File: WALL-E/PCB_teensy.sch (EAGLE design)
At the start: 50 parts

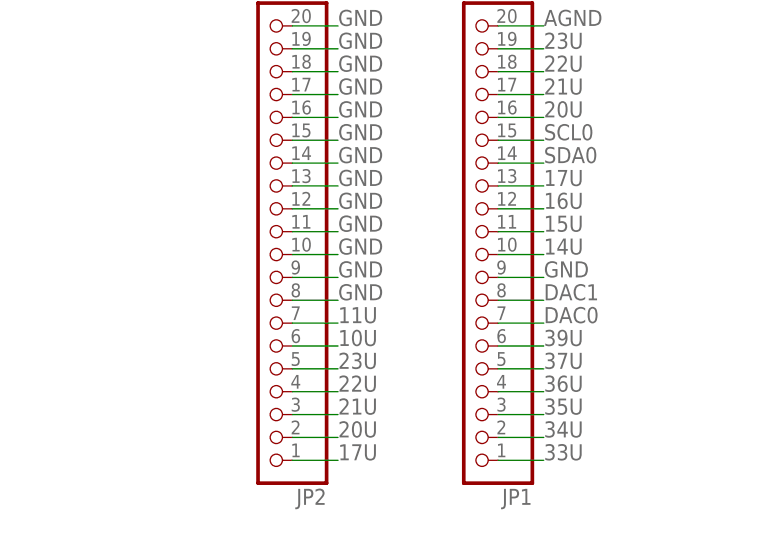
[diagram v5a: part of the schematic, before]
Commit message: Rewired the pins for JP2 to make the pins be physically closer to the teensy.
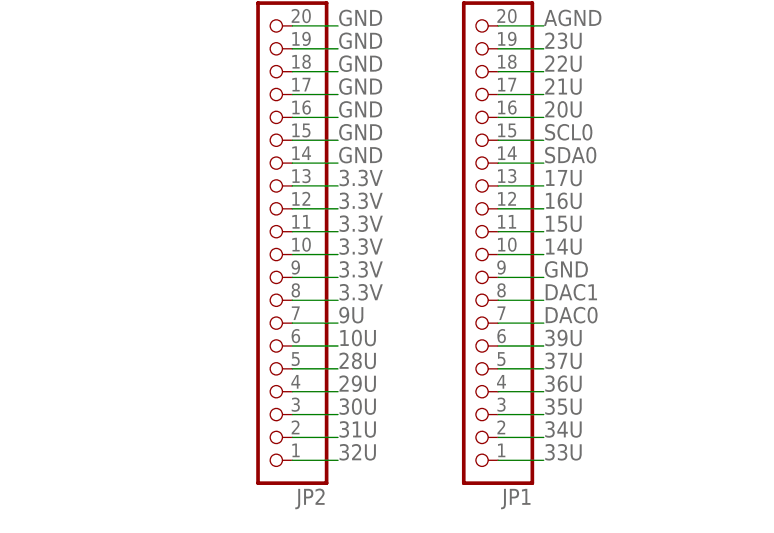
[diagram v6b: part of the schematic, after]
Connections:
- net 11U: no longer JP2.7
- net 17U: no longer JP2.1
- net 20U: no longer JP2.2
- net 21U: no longer JP2.3
- net 22U: no longer JP2.4
- net 23U: no longer JP2.5
- net 28U: now also JP2.5
- net 29U: now also JP2.4
- net 3.3V: now also JP2.10, JP2.11, JP2.12, JP2.13, JP2.8, JP2.9
- net 30U: now also JP2.3
- net 31U: now also JP2.2
- net 32U: now also JP2.1
- net 9U: now also JP2.7
- net GND: no longer JP2.10, JP2.11, JP2.12, JP2.13, JP2.8, JP2.9
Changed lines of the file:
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@@
-</segment>
-<segment>
-<pinref part="JP2" gate="A" pin="8"/>
-<wire x1="-96.52" y1="-35.56" x2="-91.44" y2="-35.56" width="0.1524" layer="91"/>
-<label x="-91.44" y="-35.56" size="1.778" layer="95"/>
-</segment>
-<segment>
-<wire x1="-96.52" y1="-33.02" x2="-91.44" y2="-33.02" width="0.1524" layer="91"/>
-<label x="-91.44" y="-33.02" size="1.778" layer="95"/>
-<pinref part="JP2" gate="A" pin="9"/>
-</segment>
-<segment>
-<wire x1="-96.52" y1="-30.48" x2="-91.44" y2="-30.48" width="0.1524" layer="91"/>
-<label x="-91.44" y="-30.48" size="1.778" layer="95"/>
-<pinref part="JP2" gate="A" pin="10"/>
-</segment>
-<segment>
-<wire x1="-96.52" y1="-27.94" x2="-91.44" y2="-27.94" width="0.1524" layer="91"/>
-<label x="-91.44" y="-27.94" size="1.778" layer="95"/>
-<pinref part="JP2" gate="A" pin="11"/>
-</segment>
-<segment>
-<wire x1="-96.52" y1="-25.4" x2="-91.44" y2="-25.4" width="0.1524" layer="91"/>
-<label x="-91.44" y="-25.4" size="1.778" layer="95"/>
-<pinref part="JP2" gate="A" pin="12"/>
-</segment>
-<segment>
-<wire x1="-96.52" y1="-22.86" x2="-91.44" y2="-22.86" width="0.1524" layer="91"/>
-<label x="-91.44" y="-22.86" size="1.778" layer="95"/>
-<pinref part="JP2" gate="A" pin="13"/>
 </segment>
 <segment>
@@
 <label x="78.74" y="60.96" size="1.778" layer="95"/>
 </segment>
+<segment>
+<pinref part="JP2" gate="A" pin="8"/>
+<wire x1="-96.52" y1="-35.56" x2="-91.44" y2="-35.56" width="0.1524" layer="91"/>
+<label x="-91.44" y="-35.56" size="1.778" layer="95"/>
+</segment>
+<segment>
+<wire x1="-96.52" y1="-33.02" x2="-91.44" y2="-33.02" width="0.1524" layer="91"/>
+<label x="-91.44" y="-33.02" size="1.778" layer="95"/>
+<pinref part="JP2" gate="A" pin="9"/>
+</segment>
+<segment>
+<wire x1="-96.52" y1="-30.48" x2="-91.44" y2="-30.48" width="0.1524" layer="91"/>
+<label x="-91.44" y="-30.48" size="1.778" layer="95"/>
+<pinref part="JP2" gate="A" pin="10"/>
+</segment>
+<segment>
+<wire x1="-96.52" y1="-27.94" x2="-91.44" y2="-27.94" width="0.1524" layer="91"/>
+<label x="-91.44" y="-27.94" size="1.778" layer="95"/>
+<pinref part="JP2" gate="A" pin="11"/>
+</segment>
+<segment>
+<wire x1="-96.52" y1="-25.4" x2="-91.44" y2="-25.4" width="0.1524" layer="91"/>
+<label x="-91.44" y="-25.4" size="1.778" layer="95"/>
+<pinref part="JP2" gate="A" pin="12"/>
+</segment>
+<segment>
+<wire x1="-96.52" y1="-22.86" x2="-91.44" y2="-22.86" width="0.1524" layer="91"/>
+<label x="-91.44" y="-22.86" size="1.778" layer="95"/>
+<pinref part="JP2" gate="A" pin="13"/>
+</segment>
 </net>
 <net name="N$8" class="0">
@@
 <label x="-35.56" y="15.24" size="1.778" layer="95"/>
 </segment>
+<segment>
+<pinref part="JP2" gate="A" pin="5"/>
+<wire x1="-96.52" y1="-43.18" x2="-91.44" y2="-43.18" width="0.1524" layer="91"/>
+<label x="-91.44" y="-43.18" size="1.778" layer="95"/>
+</segment>
 </net>
 <net name="29U" class="0">
@@
 <label x="-35.56" y="12.7" size="1.778" layer="95"/>
 </segment>
+<segment>
+<pinref part="JP2" gate="A" pin="4"/>
+<wire x1="-96.52" y1="-45.72" x2="-91.44" y2="-45.72" width="0.1524" layer="91"/>
+<label x="-91.44" y="-45.72" size="1.778" layer="95"/>
+</segment>
 </net>
 <net name="30U" class="0">
@@
 <label x="-35.56" y="10.16" size="1.778" layer="95"/>
 </segment>
+<segment>
+<pinref part="JP2" gate="A" pin="3"/>
+<wire x1="-96.52" y1="-48.26" x2="-91.44" y2="-48.26" width="0.1524" layer="91"/>
+<label x="-91.44" y="-48.26" size="1.778" layer="95"/>
+</segment>
 </net>
 <net name="31U" class="0">
@@
 <label x="-35.56" y="7.62" size="1.778" layer="95"/>
 </segment>
+<segment>
+<pinref part="JP2" gate="A" pin="2"/>
+<wire x1="-96.52" y1="-50.8" x2="-91.44" y2="-50.8" width="0.1524" layer="91"/>
+<label x="-91.44" y="-50.8" size="1.778" layer="95"/>
+</segment>
 </net>
 <net name="32U" class="0">
@@
 <label x="-35.56" y="5.08" size="1.778" layer="95"/>
 </segment>
+<segment>
+<pinref part="JP2" gate="A" pin="1"/>
+<wire x1="-96.52" y1="-53.34" x2="-91.44" y2="-53.34" width="0.1524" layer="91"/>
+<label x="-91.44" y="-53.34" size="1.778" layer="95"/>
+</segment>
 </net>
 <net name="33U" class="0">
@@
 </segment>
 <segment>
-<pinref part="JP2" gate="A" pin="1"/>
-<wire x1="-96.52" y1="-53.34" x2="-91.44" y2="-53.34" width="0.1524" layer="91"/>
-<label x="-91.44" y="-53.34" size="1.778" layer="95"/>
-</segment>
-<segment>
 <pinref part="JP1" gate="A" pin="13"/>
 <wire x1="-73.66" y1="-22.86" x2="-68.58" y2="-22.86" width="0.1524" layer="91"/>
@@
 </segment>
 <segment>
-<pinref part="JP2" gate="A" pin="2"/>
-<wire x1="-96.52" y1="-50.8" x2="-91.44" y2="-50.8" width="0.1524" layer="91"/>
-<label x="-91.44" y="-50.8" size="1.778" layer="95"/>
-</segment>
-<segment>
 <pinref part="JP1" gate="A" pin="16"/>
 <wire x1="-73.66" y1="-15.24" x2="-68.58" y2="-15.24" width="0.1524" layer="91"/>
@@
 </segment>
 <segment>
-<pinref part="JP2" gate="A" pin="3"/>
-<wire x1="-96.52" y1="-48.26" x2="-91.44" y2="-48.26" width="0.1524" layer="91"/>
-<label x="-91.44" y="-48.26" size="1.778" layer="95"/>
-</segment>
-<segment>
 <pinref part="JP1" gate="A" pin="17"/>
 <wire x1="-73.66" y1="-12.7" x2="-68.58" y2="-12.7" width="0.1524" layer="91"/>
@@
 </segment>
 <segment>
-<pinref part="JP2" gate="A" pin="4"/>
-<wire x1="-96.52" y1="-45.72" x2="-91.44" y2="-45.72" width="0.1524" layer="91"/>
-<label x="-91.44" y="-45.72" size="1.778" layer="95"/>
-</segment>
-<segment>
 <pinref part="JP1" gate="A" pin="18"/>
 <wire x1="-73.66" y1="-10.16" x2="-68.58" y2="-10.16" width="0.1524" layer="91"/>
@@
 </segment>
 <segment>
-<pinref part="JP2" gate="A" pin="5"/>
-<wire x1="-96.52" y1="-43.18" x2="-91.44" y2="-43.18" width="0.1524" layer="91"/>
-<label x="-91.44" y="-43.18" size="1.778" layer="95"/>
-</segment>
-<segment>
 <pinref part="JP1" gate="A" pin="19"/>
 <wire x1="-73.66" y1="-7.62" x2="-68.58" y2="-7.62" width="0.1524" layer="91"/>
@@
 <label x="-35.56" y="38.1" size="1.778" layer="95"/>
 </segment>
+<segment>
+<pinref part="JP2" gate="A" pin="7"/>
+<wire x1="-96.52" y1="-38.1" x2="-91.44" y2="-38.1" width="0.1524" layer="91"/>
+<label x="-91.44" y="-38.1" size="1.778" layer="95"/>
+</segment>
 </net>
 <net name="10U" class="0">
@@
 <label x="-7.62" y="83.82" size="1.778" layer="95"/>
 </segment>
-<segment>
-<pinref part="JP2" gate="A" pin="7"/>
-<wire x1="-96.52" y1="-38.1" x2="-91.44" y2="-38.1" width="0.1524" layer="91"/>
-<label x="-91.44" y="-38.1" size="1.778" layer="95"/>
-</segment>
-</net>
+</net>

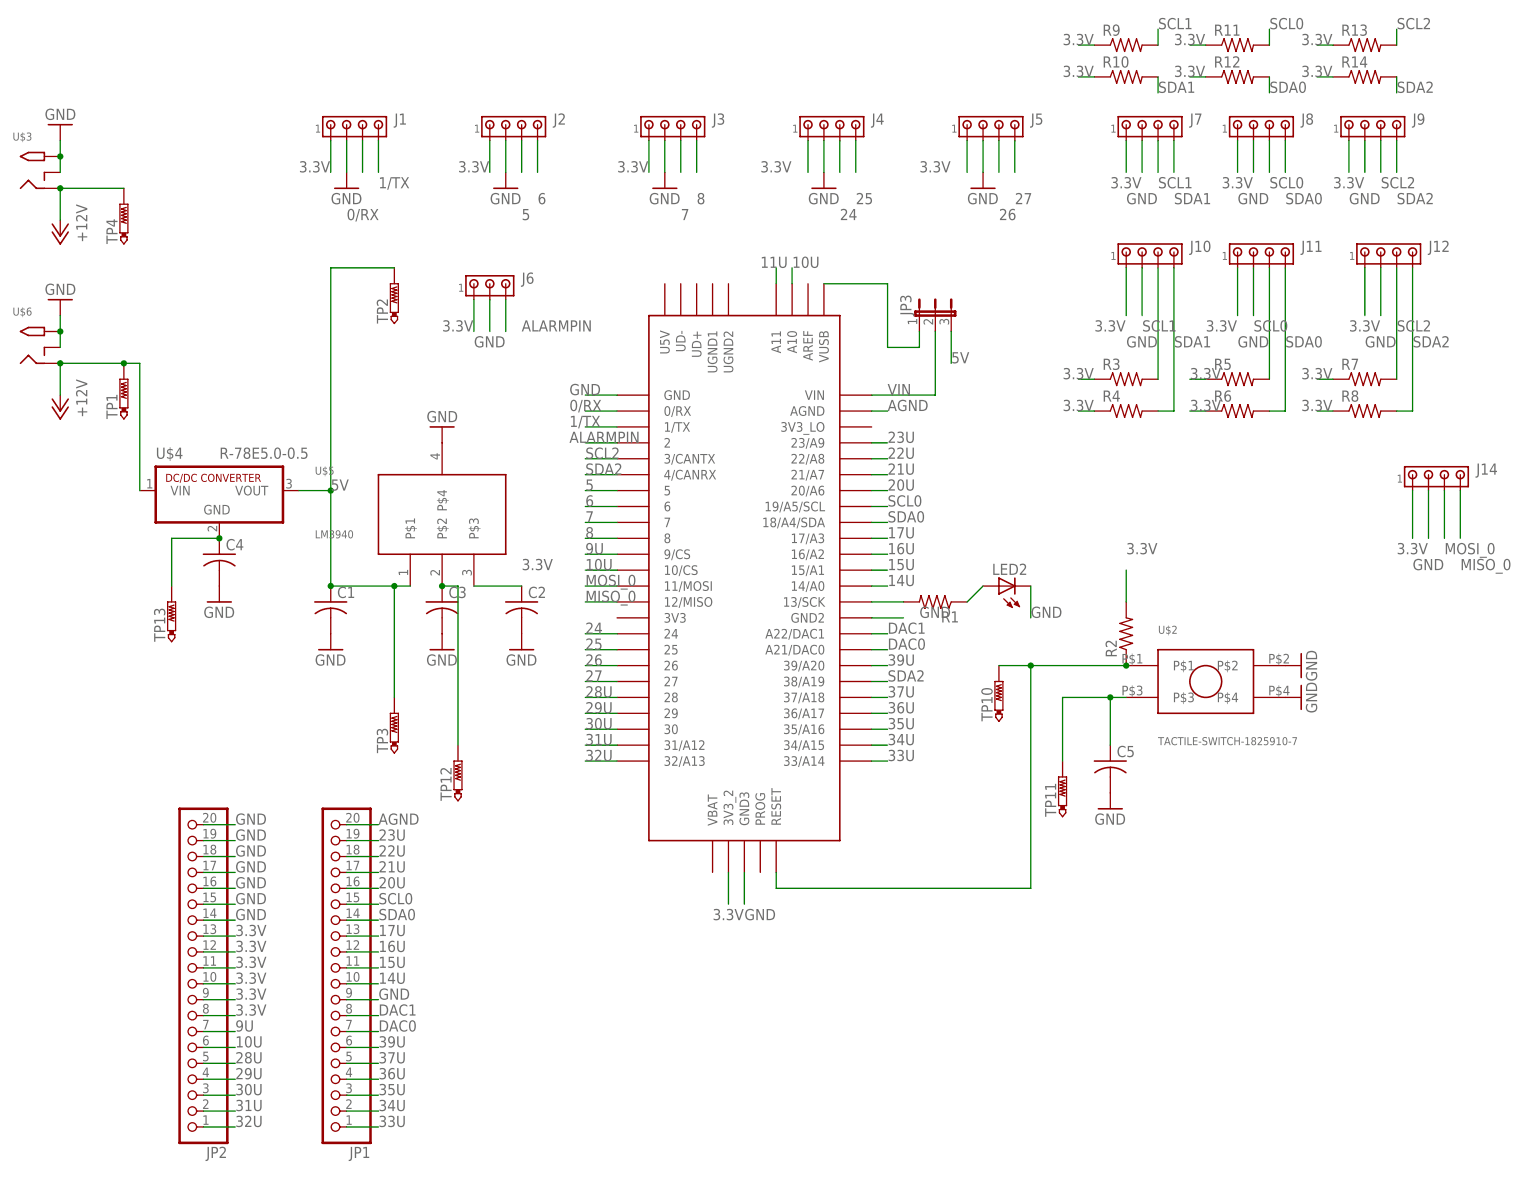
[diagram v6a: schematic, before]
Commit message: Routed all the header pins closest to Teensy and resistors.
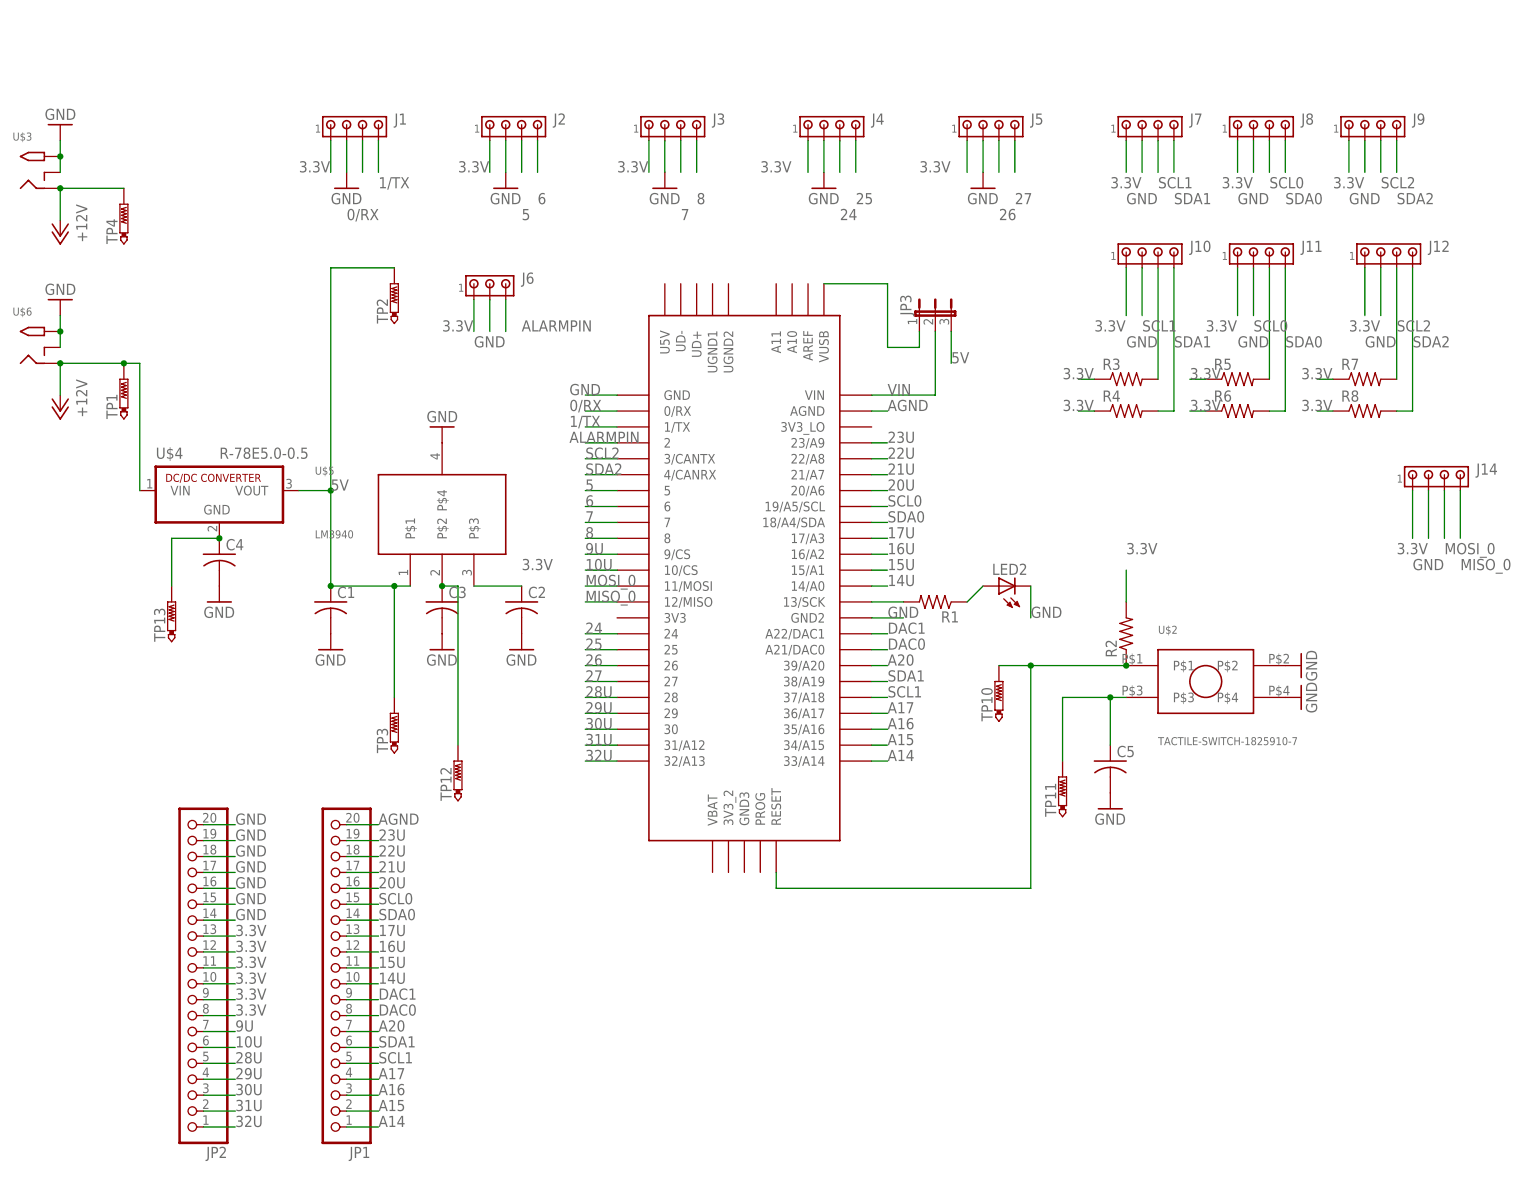
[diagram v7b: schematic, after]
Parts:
- removed R10, R11, R12, R13, R14, R9: (no value), adafruit:R-US_R0805
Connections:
- net 33U renamed A14
- net 34U renamed A15
- net 35U renamed A16
- net 36U renamed A17
- removed net 11U: U$1.A11
- removed net 37U: JP1.5, U$1.37/A18
- removed net 39U: JP1.6, U$1.39/A20
- new net A20: JP1.7, U$1.39/A20
- net 10U: no longer U$1.A10
- net 3.3V: no longer R10.1, R11.1, R12.1, R13.1, R14.1, R9.1, U$1.3V3_2
- net DAC0: now also JP1.8; no longer JP1.7
- net DAC1: now also JP1.9; no longer JP1.8
- net GND: no longer JP1.9, U$1.GND3
- net SCL0: no longer R11.2
- net SCL1: now also JP1.5, U$1.37/A18; no longer R9.2
- net SCL2: no longer R13.2
- net SDA0: no longer R12.2
- net SDA1: now also JP1.6, U$1.38/A19; no longer R10.2
- net SDA2: no longer R14.2, U$1.38/A19
